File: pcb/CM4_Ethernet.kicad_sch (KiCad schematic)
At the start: 14 parts, among them U1 TPD4EUSB30, U2 TPD4EUSB30, U3 MagJack-A70-112-331N126, U7 74LVC1G07SE-7

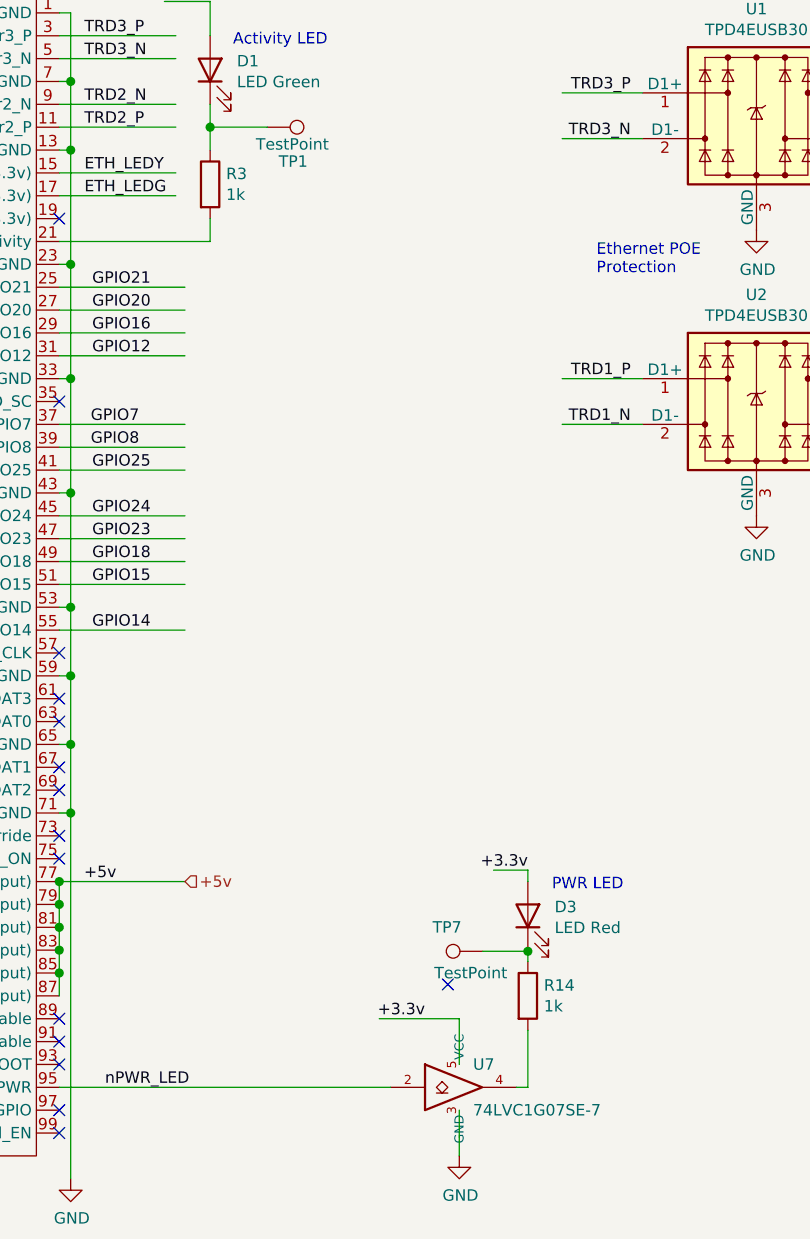
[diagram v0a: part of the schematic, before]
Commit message: - USB sound wired
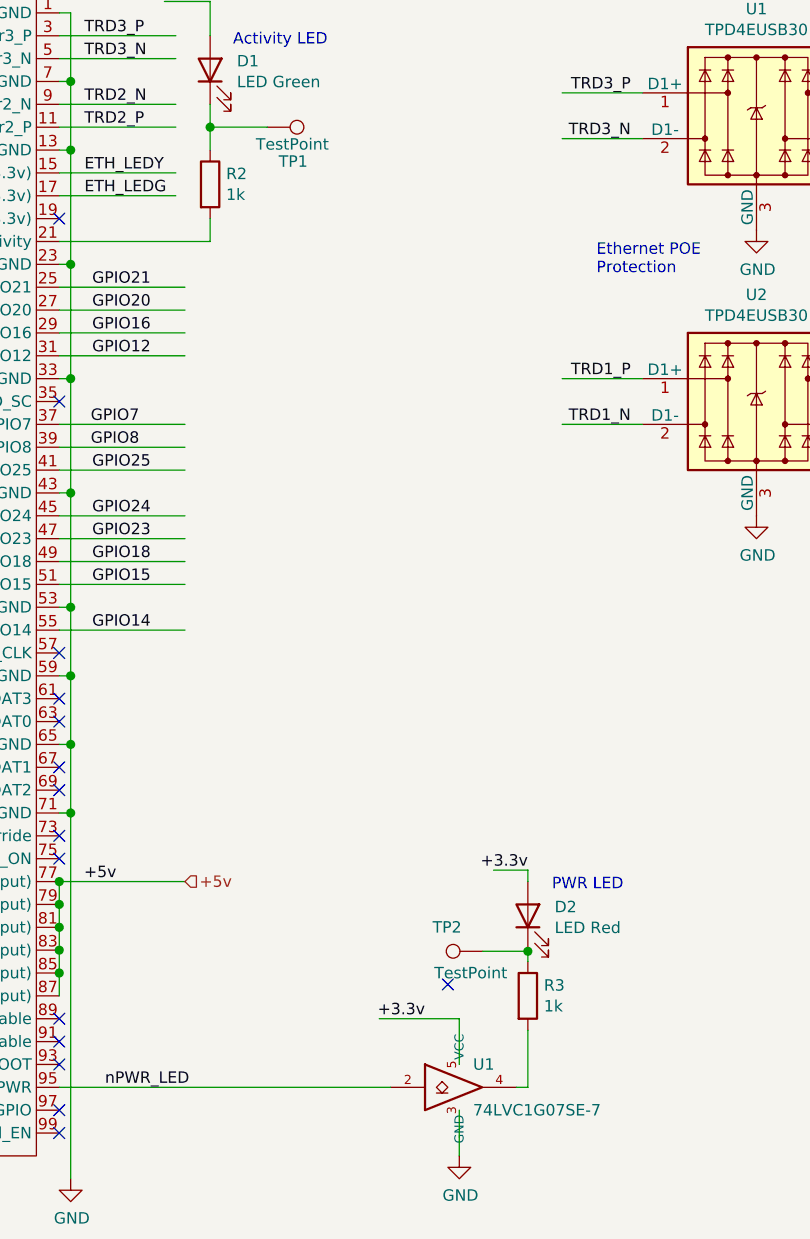
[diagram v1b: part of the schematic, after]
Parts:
- renumbered D3 to D2, R3 to R2, R14 to R3, TP7 to TP2, U7 to U1
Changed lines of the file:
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@@
         )
         (path "/c639bae0-d26f-43ee-9e8c-ca060284bd0b/0d83f7c4-6343-47e0-83de-c41ded3b9d5e"
+          (reference "U3") (unit 1)
+        )
+      )
+      (project "CM4IOv5"
+        (path "/e63e39d7-6ac0-4ffd-8aa3-1841a4541b55/00000000-0000-0000-0000-00005cff706a"
           (reference "U2") (unit 1)
         )
       )
-      (project "CM4IOv5"
-        (path "/e63e39d7-6ac0-4ffd-8aa3-1841a4541b55/00000000-0000-0000-0000-00005cff706a"
-          (reference "U2") (unit 1)
-        )
-      )
     )
   )
   (symbol (lib_id "Device:R") (at 129.794 48.26 0) (unit 1)
     (in_bom yes) (on_board yes) (dnp no)
-    (property "Reference" "R3" (at 131.572 47.0916 0)
+    (property "Reference" "R2" (at 131.572 47.0916 0)
       (effects (font (size 1.27 1.27)) (justify left))
     )
@@
       (project "VolumioAmp"
         (path "/c639bae0-d26f-43ee-9e8c-ca060284bd0b/0d83f7c4-6343-47e0-83de-c41ded3b9d5e"
-          (reference "R3") (unit 1)
+          (reference "R2") (unit 1)
         )
       )
@@
   (symbol (lib_id "Device:LED") (at 165.1 129.54 90) (unit 1)
     (in_bom yes) (on_board yes) (dnp no)
-    (property "Reference" "D3" (at 168.0718 128.5494 90)
+    (property "Reference" "D2" (at 168.0718 128.5494 90)
       (effects (font (size 1.27 1.27)) (justify right))
     )
@@
       (project "VolumioAmp"
         (path "/c639bae0-d26f-43ee-9e8c-ca060284bd0b/0d83f7c4-6343-47e0-83de-c41ded3b9d5e"
-          (reference "D3") (unit 1)
+          (reference "D2") (unit 1)
         )
       )
@@
   (symbol (lib_id "CM4IO:74LVC1G07_copy") (at 157.48 148.59 0) (unit 1)
     (in_bom yes) (on_board yes) (dnp no)
-    (property "Reference" "U7" (at 159.004 146.05 0)
+    (property "Reference" "U1" (at 159.004 146.05 0)
       (effects (font (size 1.27 1.27)) (justify left))
     )
@@
       (project "VolumioAmp"
         (path "/c639bae0-d26f-43ee-9e8c-ca060284bd0b/0d83f7c4-6343-47e0-83de-c41ded3b9d5e"
-          (reference "U7") (unit 1)
+          (reference "U1") (unit 1)
         )
       )
@@
         )
         (path "/c639bae0-d26f-43ee-9e8c-ca060284bd0b/0d83f7c4-6343-47e0-83de-c41ded3b9d5e"
-          (reference "R2") (unit 1)
+          (reference "R5") (unit 1)
         )
       )
@@
   (symbol (lib_id "Connector:TestPoint") (at 160.0962 133.477 90) (unit 1)
     (in_bom yes) (on_board yes) (dnp no)
-    (property "Reference" "TP7" (at 157.734 130.81 90)
+    (property "Reference" "TP2" (at 157.734 130.81 90)
       (effects (font (size 1.27 1.27)) (justify left))
     )
@@
       (project "VolumioAmp"
         (path "/c639bae0-d26f-43ee-9e8c-ca060284bd0b/0d83f7c4-6343-47e0-83de-c41ded3b9d5e"
-          (reference "TP7") (unit 1)
+          (reference "TP2") (unit 1)
         )
       )
@@
         )
         (path "/c639bae0-d26f-43ee-9e8c-ca060284bd0b/0d83f7c4-6343-47e0-83de-c41ded3b9d5e"
-          (reference "#PWR04") (unit 1)
+          (reference "#PWR010") (unit 1)
         )
       )
@@
         )
         (path "/c639bae0-d26f-43ee-9e8c-ca060284bd0b/0d83f7c4-6343-47e0-83de-c41ded3b9d5e"
-          (reference "#PWR01") (unit 1)
+          (reference "#PWR07") (unit 1)
         )
       )
@@
   (symbol (lib_id "power:GND") (at 157.48 156.21 0) (unit 1)
     (in_bom yes) (on_board yes) (dnp no)
-    (property "Reference" "#PWR023" (at 157.48 162.56 0)
+    (property "Reference" "#PWR06" (at 157.48 162.56 0)
       (effects (font (size 1.27 1.27)) hide)
     )
@@
       (project "VolumioAmp"
         (path "/c639bae0-d26f-43ee-9e8c-ca060284bd0b/0d83f7c4-6343-47e0-83de-c41ded3b9d5e"
-          (reference "#PWR023") (unit 1)
+          (reference "#PWR06") (unit 1)
         )
       )
@@
         )
         (path "/c639bae0-d26f-43ee-9e8c-ca060284bd0b/0d83f7c4-6343-47e0-83de-c41ded3b9d5e"
-          (reference "U3") (unit 1)
+          (reference "U4") (unit 1)
         )
       )
@@
         )
         (path "/c639bae0-d26f-43ee-9e8c-ca060284bd0b/0d83f7c4-6343-47e0-83de-c41ded3b9d5e"
-          (reference "#PWR02") (unit 1)
+          (reference "#PWR08") (unit 1)
         )
       )
@@
         )
         (path "/c639bae0-d26f-43ee-9e8c-ca060284bd0b/0d83f7c4-6343-47e0-83de-c41ded3b9d5e"
+          (reference "U2") (unit 1)
+        )
+      )
+      (project "CM4IOv5"
+        (path "/e63e39d7-6ac0-4ffd-8aa3-1841a4541b55/00000000-0000-0000-0000-00005cff706a"
           (reference "U1") (unit 1)
         )
       )
-      (project "CM4IOv5"
-        (path "/e63e39d7-6ac0-4ffd-8aa3-1841a4541b55/00000000-0000-0000-0000-00005cff706a"
-          (reference "U1") (unit 1)
-        )
-      )
     )
   )
@@
   (symbol (lib_id "power:GND") (at 50.8 158.75 0) (unit 1)
     (in_bom yes) (on_board yes) (dnp no)
-    (property "Reference" "#PWR05" (at 50.8 165.1 0)
+    (property "Reference" "#PWR04" (at 50.8 165.1 0)
       (effects (font (size 1.27 1.27)) hide)
     )
@@
       (project "VolumioAmp"
         (path "/c639bae0-d26f-43ee-9e8c-ca060284bd0b/0d83f7c4-6343-47e0-83de-c41ded3b9d5e"
+          (reference "#PWR04") (unit 1)
+        )
+      )
+      (project "CM4IOv5"
+        (path "/e63e39d7-6ac0-4ffd-8aa3-1841a4541b55/00000000-0000-0000-0000-00005cff706a"
+          (reference "#PWR0104") (unit 1)
+        )
+      )
+    )
+  )
+  (symbol (lib_id "power:GND") (at 114.3 158.75 0) (unit 1)
+    (in_bom yes) (on_board yes) (dnp no)
+    (property "Reference" "#PWR05" (at 114.3 165.1 0)
+      (effects (font (size 1.27 1.27)) hide)
+    )
+    (property "Value" "GND" (at 114.427 163.1442 0)
+      (effects (font (size 1.27 1.27)))
+    )
+    (property "Footprint" "" (at 114.3 158.75 0)
+      (effects (font (size 1.27 1.27)) hide)
+    )
+    (property "Datasheet" "" (at 114.3 158.75 0)
+      (effects (font (size 1.27 1.27)) hide)
+    )
+    (pin "1")
+    (instances
+      (project "VolumioAmp"
+        (path "/c639bae0-d26f-43ee-9e8c-ca060284bd0b/0d83f7c4-6343-47e0-83de-c41ded3b9d5e"
           (reference "#PWR05") (unit 1)
-        )
-      )
-      (project "CM4IOv5"
-        (path "/e63e39d7-6ac0-4ffd-8aa3-1841a4541b55/00000000-0000-0000-0000-00005cff706a"
-          (reference "#PWR0104") (unit 1)
-        )
-      )
-    )
-  )
-  (symbol (lib_id "power:GND") (at 114.3 158.75 0) (unit 1)
-    (in_bom yes) (on_board yes) (dnp no)
-    (property "Reference" "#PWR06" (at 114.3 165.1 0)
-      (effects (font (size 1.27 1.27)) hide)
-    )
-    (property "Value" "GND" (at 114.427 163.1442 0)
-      (effects (font (size 1.27 1.27)))
-    )
-    (property "Footprint" "" (at 114.3 158.75 0)
-      (effects (font (size 1.27 1.27)) hide)
-    )
-    (property "Datasheet" "" (at 114.3 158.75 0)
-      (effects (font (size 1.27 1.27)) hide)
-    )
-    (pin "1")
-    (instances
-      (project "VolumioAmp"
-        (path "/c639bae0-d26f-43ee-9e8c-ca060284bd0b/0d83f7c4-6343-47e0-83de-c41ded3b9d5e"
-          (reference "#PWR06") (unit 1)
         )
       )
@@
         )
         (path "/c639bae0-d26f-43ee-9e8c-ca060284bd0b/0d83f7c4-6343-47e0-83de-c41ded3b9d5e"
-          (reference "R1") (unit 1)
+          (reference "R4") (unit 1)
         )
       )
@@
   (symbol (lib_id "Device:R") (at 165.1 138.43 0) (unit 1)
     (in_bom yes) (on_board yes) (dnp no)
-    (property "Reference" "R14" (at 166.878 137.2616 0)
+    (property "Reference" "R3" (at 166.878 137.2616 0)
       (effects (font (size 1.27 1.27)) (justify left))
     )
@@
       (project "VolumioAmp"
         (path "/c639bae0-d26f-43ee-9e8c-ca060284bd0b/0d83f7c4-6343-47e0-83de-c41ded3b9d5e"
-          (reference "R14") (unit 1)
+          (reference "R3") (unit 1)
         )
       )
@@
         )
         (path "/c639bae0-d26f-43ee-9e8c-ca060284bd0b/0d83f7c4-6343-47e0-83de-c41ded3b9d5e"
-          (reference "#PWR03") (unit 1)
-        )
-      )
+          (reference "#PWR09") (unit 1)
+        )
+      )

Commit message: - work in progress
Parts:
- added JP3: LRCK, symbol Jumper:SolderJumper_2_Open
- added JP3: D, symbol Jumper:SolderJumper_2_Open
- added JP3: BCK, symbol Jumper:SolderJumper_2_Open
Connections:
- net GPIO18: now also JP3.1 (A)
- net GPIO19: now also JP3.2 (B)
- net GPIO21: now also JP3.1 (A)
- new net I2S.BCK: JP3.2 (B)
- new net I2S.D: JP3.2 (B)
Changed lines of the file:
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@@
   (junction (at 229.87 97.79) (diameter 1.016) (color 0 0 0 0)
   )
+  (junction (at 138.43 90.17) (diameter 0) (color 0 0 0 0)
+  )
   (junction (at 228.6 46.99) (diameter 1.016) (color 0 0 0 0)
   )
@@
   (junction (at 114.3 95.25) (diameter 1.016) (color 0 0 0 0)
   )
+  (junction (at 138.43 59.69) (diameter 0) (color 0 0 0 0)
+  )
   (junction (at 114.3 57.15) (diameter 1.016) (color 0 0 0 0)
   )
   (junction (at 46.99 133.35) (diameter 0) (color 0 0 0 0)
+  )
+  (junction (at 27.94 59.69) (diameter 0) (color 0 0 0 0)
   )
   (junction (at 114.3 118.11) (diameter 1.016) (color 0 0 0 0)
@@
   (no_connect (at 229.87 72.39))
   (no_connect (at 113.03 72.39))
+  (bus_entry (at 144.78 57.15) (size -2.54 2.54)
+    (stroke (width 0) (type default))
+  )
+  (bus_entry (at 20.32 57.15) (size 2.54 2.54)
+    (stroke (width 0) (type default))
+  )
+  (bus_entry (at 144.78 87.63) (size -2.54 2.54)
+    (stroke (width 0) (type default))
+  )
   (wire (pts (xy 52.07 135.89) (xy 52.07 133.35))
     (stroke (width 0) (type solid))
@@
     (stroke (width 0) (type solid))
   )
+  (wire (pts (xy 29.21 59.69) (xy 27.94 59.69))
+    (stroke (width 0) (type default))
+  )
   (wire (pts (xy 52.07 44.45) (xy 50.8 44.45))
     (stroke (width 0) (type solid))
@@
     (stroke (width 0) (type solid))
   )
+  (bus (pts (xy 144.78 57.15) (xy 144.78 87.63))
+    (stroke (width 0) (type default))
+  )
   (wire (pts (xy 220.98 39.37) (xy 229.87 39.37))
     (stroke (width 0) (type solid))
@@
     (stroke (width 0) (type solid))
   )
+  (wire (pts (xy 138.43 90.17) (xy 142.24 90.17))
+    (stroke (width 0) (type default))
+  )
   (wire (pts (xy 38.1 57.15) (xy 52.07 57.15))
     (stroke (width 0) (type solid))
@@
     (stroke (width 0) (type default))
   )
+  (wire (pts (xy 113.03 59.69) (xy 130.81 59.69))
+    (stroke (width 0) (type solid))
+  )
   (wire (pts (xy 168.91 43.18) (xy 177.8 43.18))
     (stroke (width 0) (type solid))
@@
     (stroke (width 0) (type solid))
   )
+  (bus (pts (xy 20.32 20.32) (xy 20.32 57.15))
+    (stroke (width 0) (type default))
+  )
   (wire (pts (xy 113.03 41.91) (xy 125.984 41.91))
     (stroke (width 0) (type solid))
@@
     (stroke (width 0) (type solid))
   )
+  (wire (pts (xy 35.56 59.69) (xy 52.07 59.69))
+    (stroke (width 0) (type default))
+  )
   (wire (pts (xy 220.98 82.55) (xy 228.6 82.55))
     (stroke (width 0) (type solid))
@@
     (stroke (width 0) (type solid))
   )
+  (bus (pts (xy 144.78 20.32) (xy 144.78 57.15))
+    (stroke (width 0) (type default))
+  )
+  (wire (pts (xy 137.16 90.17) (xy 138.43 90.17))
+    (stroke (width 0) (type default))
+  )
   (wire (pts (xy 38.1 82.55) (xy 52.07 82.55))
     (stroke (width 0) (type solid))
@@
     (stroke (width 0) (type solid))
   )
+  (wire (pts (xy 142.24 59.69) (xy 138.43 59.69))
+    (stroke (width 0) (type default))
+  )
   (wire (pts (xy 38.1 64.77) (xy 52.07 64.77))
     (stroke (width 0) (type solid))
@@
     (stroke (width 0) (type solid))
   )
-  (wire (pts (xy 38.1 59.69) (xy 52.07 59.69))
-    (stroke (width 0) (type solid))
+  (bus (pts (xy 144.78 20.32) (xy 20.32 20.32))
+    (stroke (width 0) (type default))
   )
   (wire (pts (xy 165.1 148.59) (xy 163.83 148.59))
@@
     (stroke (width 0) (type solid))
   )
+  (wire (pts (xy 22.86 59.69) (xy 27.94 59.69))
+    (stroke (width 0) (type default))
+  )
   (wire (pts (xy 113.03 69.85) (xy 114.3 69.85))
     (stroke (width 0) (type solid))
@@
     (stroke (width 0) (type solid))
   )
-  (wire (pts (xy 113.03 90.17) (xy 127 90.17))
-    (stroke (width 0) (type solid))
-  )
   (wire (pts (xy 114.3 95.25) (xy 114.3 102.87))
     (stroke (width 0) (type solid))
@@
     (stroke (width 0) (type solid))
   )
-  (wire (pts (xy 113.03 59.69) (xy 127 59.69))
-    (stroke (width 0) (type solid))
-  )
   (wire (pts (xy 113.03 92.71) (xy 127 92.71))
     (stroke (width 0) (type solid))
@@
     (stroke (width 0) (type solid))
   )
+  (wire (pts (xy 137.16 59.69) (xy 138.43 59.69))
+    (stroke (width 0) (type default))
+  )
   (wire (pts (xy 46.99 133.35) (xy 52.07 133.35))
     (stroke (width 0) (type solid))
@@
     (stroke (width 0) (type solid))
   )
+  (wire (pts (xy 113.03 90.17) (xy 130.81 90.17))
+    (stroke (width 0) (type solid))
+  )
   (wire (pts (xy 220.98 52.07) (xy 229.87 52.07))
     (stroke (width 0) (type solid))
+  )
+  (bus (pts (xy 144.78 87.63) (xy 144.78 106.68))
+    (stroke (width 0) (type default))
   )
   (text "Ethernet" (at 200.66 29.21 0)
@@
     (effects (font (size 1.27 1.27)) (justify right bottom))
   )
+  (label "I2S.BCK" (at 137.16 90.17 0)
+    (effects (font (size 1.27 1.27)) (justify left bottom))
+  )
   (label "GPIO27" (at 45.72 87.63 180) (fields_autoplaced)
     (effects (font (size 1.27 1.27)) (justify right bottom))
@@
   (label "GPIO19" (at 45.72 59.69 180) (fields_autoplaced)
     (effects (font (size 1.27 1.27)) (justify right bottom))
+  )
+  (label "I2S.LRCK" (at 21.59 58.42 0)
+    (effects (font (size 1.27 1.27)) (justify left bottom))
   )
   (label "TRD2_P" (at 115.824 41.91 0) (fields_autoplaced)
@@
     (effects (font (size 1.27 1.27)) (justify left bottom))
   )
+  (label "I2S{LRCK BCK MCK D}" (at 144.78 92.71 0) (fields_autoplaced)
+    (effects (font (size 1.27 1.27)) (justify left bottom))
+  )
   (label "ETH_LEDG" (at 210.82 85.09 180) (fields_autoplaced)
     (effects (font (size 1.27 1.27)) (justify right bottom))
@@
     (effects (font (size 1.27 1.27)) (justify right bottom))
   )
+  (label "I2S.D" (at 137.16 59.69 0)
+    (effects (font (size 1.27 1.27)) (justify left bottom))
+  )
   (label "+3.3v" (at 45.974 133.35 180) (fields_autoplaced)
     (effects (font (size 1.27 1.27)) (justify right bottom))
@@
     (effects (font (size 1.27 1.27)) (justify right))
   )
+  (hierarchical_label "I2S" (shape input) (at 144.78 106.68 270) (fields_autoplaced)
+    (effects (font (size 1.27 1.27)) (justify right))
+  )
   (hierarchical_label "+5v" (shape input) (at 127 125.73 0) (fields_autoplaced)
     (effects (font (size 1.27 1.27)) (justify left))
@@
   (hierarchical_label "SCL0" (shape output) (at 38.1 128.27 180) (fields_autoplaced)
     (effects (font (size 1.27 1.27)) (justify right))
+  )
+  (symbol (lib_id "Jumper:SolderJumper_2_Open") (at 31.75 59.69 0) (unit 1)
+    (in_bom yes) (on_board yes) (dnp no)
+    (property "Reference" "JP3" (at 31.75 64.77 0)
+      (effects (font (size 1.27 1.27)))
+    )
+    (property "Value" "LRCK" (at 31.75 62.23 0)
+      (effects (font (size 1.27 1.27)))
+    )
+    (property "Footprint" "" (at 31.75 59.69 0)
+      (effects (font (size 1.27 1.27)) hide)
+    )
+    (property "Datasheet" "~" (at 31.75 59.69 0)
+      (effects (font (size 1.27 1.27)) hide)
+    )
+    (pin "2")
+    (pin "1")
+    (instances
+      (project "VolumioAmp"
+        (path "/c639bae0-d26f-43ee-9e8c-ca060284bd0b/93301fd2-7a6d-48be-bd24-243a1877e343"
+          (reference "JP3") (unit 1)
+        )
+        (path "/c639bae0-d26f-43ee-9e8c-ca060284bd0b/0d83f7c4-6343-47e0-83de-c41ded3b9d5e"
+          (reference "JP1") (unit 1)
+        )
+      )
+    )
   )
   (symbol (lib_id "CM4IO:TPD4EUSB30") (at 190.5 72.39 0) (unit 1)
@@
         (path "/e63e39d7-6ac0-4ffd-8aa3-1841a4541b55/00000000-0000-0000-0000-00005cff706a"
           (reference "D1") (unit 1)
+        )
+      )
+    )
+  )
+  (symbol (lib_id "Jumper:SolderJumper_2_Open") (at 134.62 59.69 0) (unit 1)
+    (in_bom yes) (on_board yes) (dnp no)
+    (property "Reference" "JP3" (at 134.62 64.77 0)
+      (effects (font (size 1.27 1.27)))
+    )
+    (property "Value" "D" (at 134.62 62.23 0)
+      (effects (font (size 1.27 1.27)))
+    )
+    (property "Footprint" "" (at 134.62 59.69 0)
+      (effects (font (size 1.27 1.27)) hide)
+    )
+    (property "Datasheet" "~" (at 134.62 59.69 0)
+      (effects (font (size 1.27 1.27)) hide)
+    )
+    (pin "2")
+    (pin "1")
+    (instances
+      (project "VolumioAmp"
+        (path "/c639bae0-d26f-43ee-9e8c-ca060284bd0b/93301fd2-7a6d-48be-bd24-243a1877e343"
+          (reference "JP3") (unit 1)
+        )
+        (path "/c639bae0-d26f-43ee-9e8c-ca060284bd0b/0d83f7c4-6343-47e0-83de-c41ded3b9d5e"
+          (reference "JP2") (unit 1)
         )
       )
@@
         )
       )
+    )
+  )
+  (symbol (lib_id "Jumper:SolderJumper_2_Open") (at 134.62 90.17 0) (unit 1)
+    (in_bom yes) (on_board yes) (dnp no)
+    (property "Reference" "JP3" (at 134.62 95.25 0)
+      (effects (font (size 1.27 1.27)))
+    )
+    (property "Value" "BCK" (at 134.62 92.71 0)
+      (effects (font (size 1.27 1.27)))
+    )
+    (property "Footprint" "" (at 134.62 90.17 0)
+      (effects (font (size 1.27 1.27)) hide)
+    )
+    (property "Datasheet" "~" (at 134.62 90.17 0)
+      (effects (font (size 1.27 1.27)) hide)
+    )
+    (pin "2")
+    (pin "1")
+    (instances
+      (project "VolumioAmp"
+        (path "/c639bae0-d26f-43ee-9e8c-ca060284bd0b/93301fd2-7a6d-48be-bd24-243a1877e343"
+          (reference "JP3") (unit 1)
+        )
+        (path "/c639bae0-d26f-43ee-9e8c-ca060284bd0b/0d83f7c4-6343-47e0-83de-c41ded3b9d5e"
+          (reference "JP3") (unit 1)
+        )
+      )
